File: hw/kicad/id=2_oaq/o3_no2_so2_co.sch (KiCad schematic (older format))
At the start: 54 parts, among them IC1 LPS22HB, IC2 SHTC1, IC3 TPS62740DSST, IC4 24AA02T-I_OT, IC5 nRF52840-QIAA-T, Q1 NMOS_DGS, Q2 NMOS_DGS, U1 SGPC3-2.5k, Y1 32MHZ, Y2 32.768K

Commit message: Update for OAQ
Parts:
- removed C1, C11, C15, C19, C20, C23, C24, C3, C5: 100nF, symbol C_Small
- removed C10, C6, C7, C9: 12pF, symbol C_Small
- removed C12, C14: 1uF, symbol C_Small
- removed C13, C17: 1pF, symbol C_Small
- removed C16, C25: 4.7uF, symbol C_Small
- removed C18: 47nF, symbol C_Small
- removed C2, C4: 10uF, Capacitors_SMD:C_0805, symbol C_Small
- removed C21: 100pF, symbol C_Small
- removed C22: 820pF, symbol C_Small
- removed C8: 1.2pF, symbol C_Small
- removed D1: red, symbol LED_Small
- removed D2: green, symbol LED_Small
- removed IC1: LPS22HB, LGA10R50P2X3_200X200X80, symbol LPS22HB
- removed IC2: SHTC1, SON100P200X200X7500-5N, symbol SHTC1
- removed IC3: TPS62740DSST, SON50P200X300X80-13N, symbol TPS62740DSST
- removed IC4: 24AA02T-I_OT, SOT95P270X145-5N, symbol 24AA02T-I_OT
- removed IC5: nRF52840-QIAA-T, AQFN73, symbol nRF52840-QIAA-T
- removed L1: 2.2uH, symbol L
- removed L2: 3.9nH, symbol L
- removed L3: 15nH, symbol L
- removed L4: 10uH, symbol L
- removed Q1, Q2: NMOS_DGS, symbol Q_NMOS_DGS
- removed R1: 10M, symbol R
- removed R10, R11, R12, R13, R5, R8, R9: 10k, symbol R_Small
- removed R2: 2M, symbol R
- removed R3, R4: 10k, symbol R
- removed R6, R7: 1k, symbol R_Small
- removed U1: SGPC3-2.5k, SON100P300X300X110-7N, symbol SGPC3-2.5k
- removed Y1: 32MHZ, FA128, symbol Q22FA12800025_FA-128_32_MHZ_8PF
- removed Y2: 32.768K, NX3215SA, symbol NX3215SA-32.768K-STD-MUA-9
- added C? (x8): 100nF, symbol C_Small
- added C? (x2): 1uF, symbol C_Small
- added IC? (x4): LMP91000SD_NOPB, SON50P400X400X80-15N, symbol LMP91000SD_NOPB
- added J? (x6): HDR_2x2mm, symbol Conn_01x02_Male
- added R? (x4): 100k, symbol R_Small
- added R? (x2): 500k, symbol R_Small
- added R? (x2): 1k, symbol R_Small
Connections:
- net labels added: 2V5, 2V7, CO, CO_EN, NO2, NO2_EN, O3, O3_EN, Reference_NO2, Reference_O3, SCL, SDA, SO2, SO2_EN, Working_NO2, Working_O3
- net labels removed: +1V8, ANT, Vbat
- wire segments 173 -> 102
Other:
- note added: "Ozone (NO2)\nSPEC Sensors"
- note added: "Ozone (O3)\nSPEC Sensors"
- note removed: "Battery power surveillance."
- note removed: "CO\n"
- note removed: "Configuration pin 0"
- note removed: "Configuration pin 1"
- note removed: "Configuration pin 2"
- note removed: "Configuration pin 3"
- note removed: "Configuration pin 4"
- note removed: "Configuration pin 5"
- note removed: "EEPROM"
- note removed: "H2S\n"
- note removed: "Module ID = 1 --> Indoor Air Quality Module (VOC)"
- note removed: "NO2\n"
- note removed: "O3"
- note removed: "Pressure Sensor"
- note removed: "SO2\n"
- note removed: "Temperature & Humidity Sensor"
- note removed: "UART RxD"
- note removed: "UART TxD"
- note removed: "VOC Sensor"
- note removed: "Vbat = 3 x AA Li-Fe 2.9Ah = 3 x 1.5V = 4.5V"

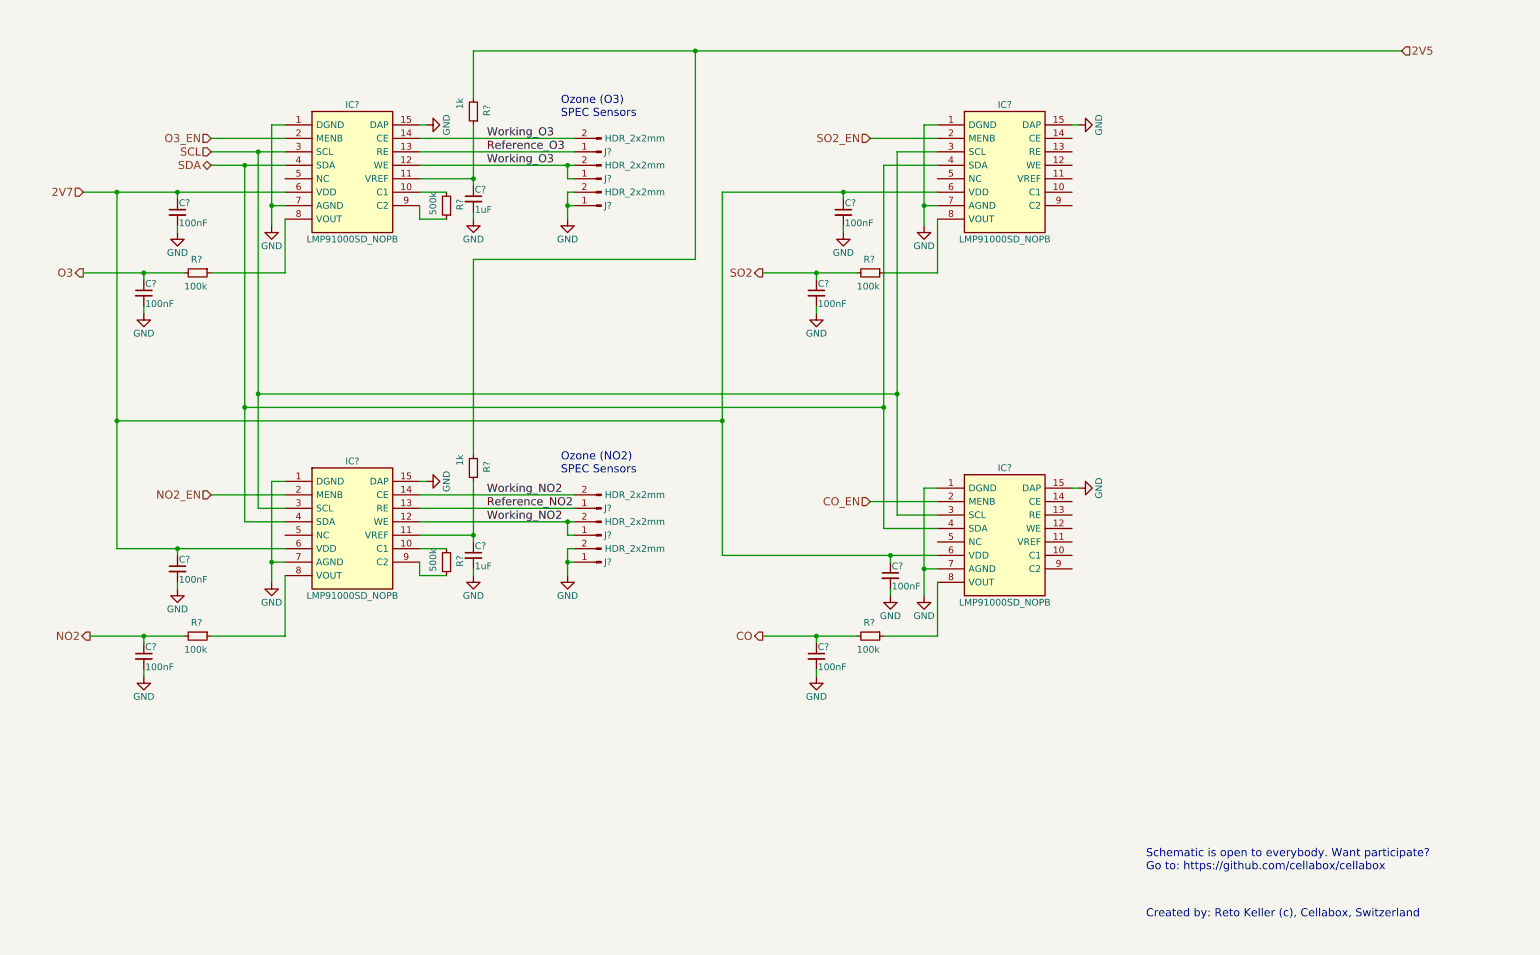
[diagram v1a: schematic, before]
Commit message: OAQ schematic updated: gains, ranges
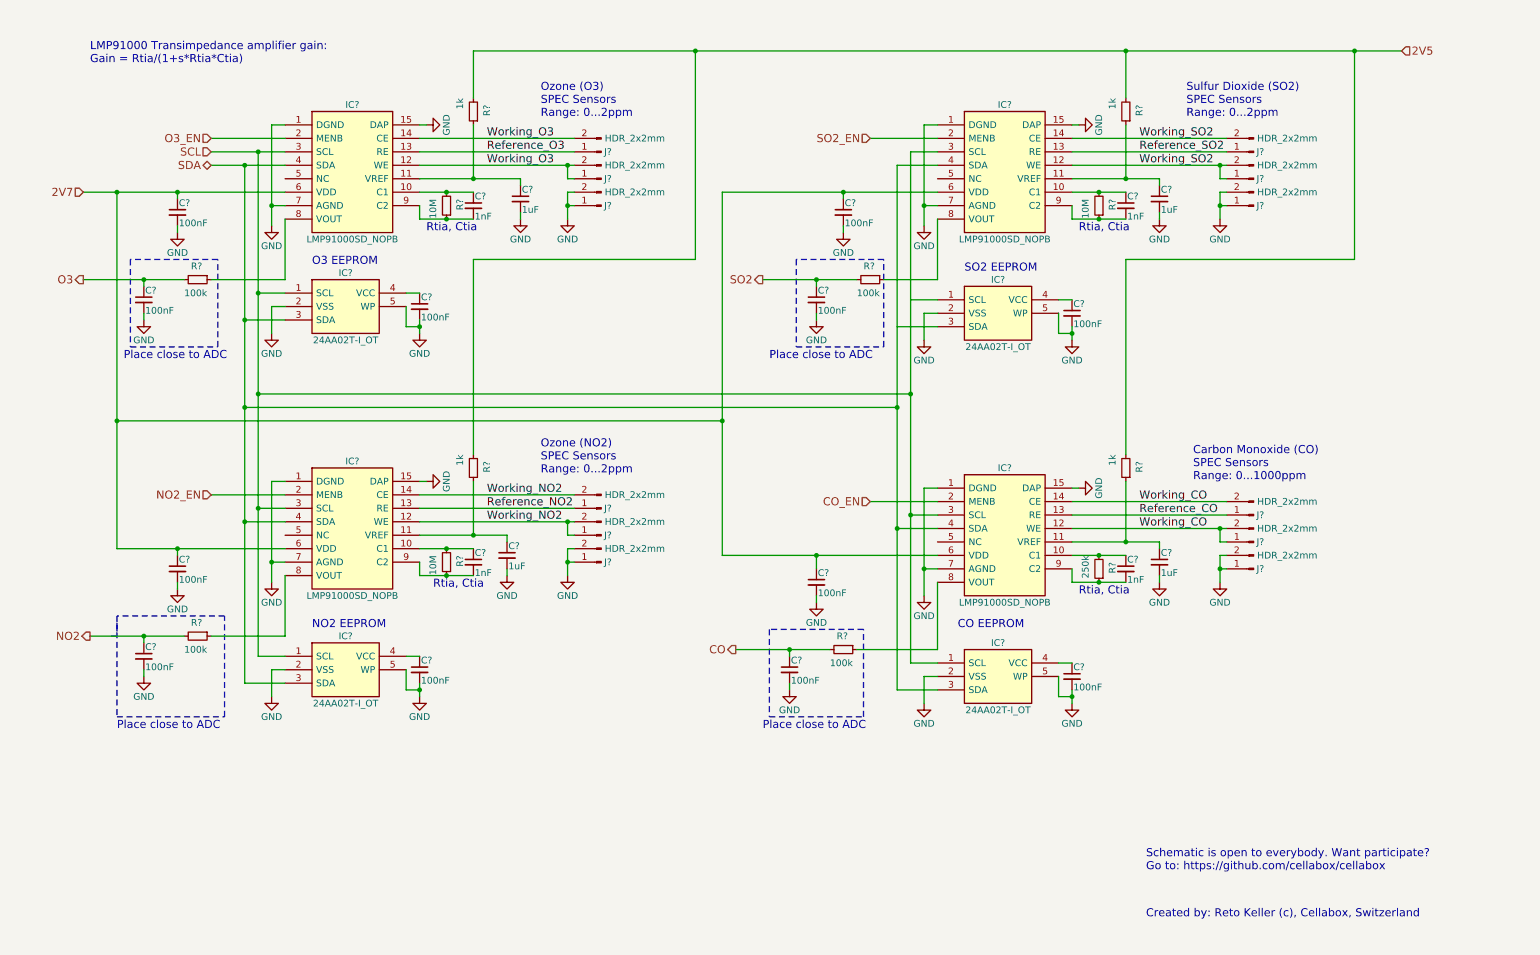
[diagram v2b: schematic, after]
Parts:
- added C? (x4): 100nF, symbol C_Small
- added C? (x4): 1nF, symbol C_Small
- added C? (x2): 1uF, symbol C_Small
- added IC? (x4): 24AA02T-I_OT, SOT95P270X145-5N, symbol 24AA02T-I_OT
- added J? (x6): HDR_2x2mm, symbol Conn_01x02_Male
- added R? (x2): 1k, symbol R_Small
- added R?: 250k, symbol R_Small
- added R?: 10M, symbol R_Small
- R? (x2): value 500k -> 10M
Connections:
- net 2V5: now also R?.2, R?.2
- net GND: now also C?.2, C?.2, C?.2, C?.2, C?.2, C?.2, IC?.2 (VSS), IC?.2 (VSS), IC?.2 (VSS), IC?.2 (VSS), IC?.5 (WP), IC?.5 (WP), IC?.5 (WP), IC?.5 (WP), J?.1 (Pin_1), J?.1 (Pin_1), J?.2 (Pin_2), J?.2 (Pin_2)
- net SCL: now also IC?.1 (SCL), IC?.1 (SCL), IC?.1 (SCL)
- net SDA: now also IC?.3 (SDA), IC?.3 (SDA), IC?.3 (SDA)
- net at IC?.10 (C1), R?.2: now also C?.1 (x2)
- net at IC?.9 (C2), R?.1: now also C?.2 (x2)
- net at IC?.10 (C1): now also C?.1, R?.2 (x2)
- net at IC?.11 (VREF): now also C?.1, R?.1 (x2)
- net Working_CO: now reaches IC?.12 (WE)
- net Working_CO: now also IC?.14 (CE), J?.1 (Pin_1), J?.2 (Pin_2), J?.2 (Pin_2)
- net Reference_CO: now reaches IC?.13 (RE)
- net Reference_CO: now also J?.1 (Pin_1)
- net at IC?.9 (C2): now also C?.2, R?.1 (x2)
- net Working_SO2: now reaches IC?.12 (WE)
- net Working_SO2: now also IC?.14 (CE), J?.1 (Pin_1), J?.2 (Pin_2), J?.2 (Pin_2)
- net Reference_SO2: now reaches IC?.13 (RE)
- net Reference_SO2: now also J?.1 (Pin_1)
- new net: C?.1, IC?.4 (VCC) (x4)
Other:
- note added: "CO EEPROM"
- note added: "Carbon Monoxide (CO)\nSPEC Sensors\nRange: 0...1000ppm"
- note added: "LMP91000 Transimpedance amplifier gain:\nGain = Rtia/(1+s*Rtia*Ctia)"
- note added: "NO2 EEPROM"
- note added: "O3 EEPROM"
- note added: "Ozone (NO2)\nSPEC Sensors\nRange: 0...2ppm"
- note added: "Ozone (O3)\nSPEC Sensors\nRange: 0...2ppm"
- note added: "Place close to ADC"
- note added: "Rtia, Ctia"
- note added: "SO2 EEPROM"
- note added: "Sulfur Dioxide (SO2)\nSPEC Sensors\nRange: 0...2ppm"
- note removed: "Ozone (NO2)\nSPEC Sensors"
- note removed: "Ozone (O3)\nSPEC Sensors"
- moved on the sheet: C?, R?

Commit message: Indoor PM2.5 module. Schematic added.
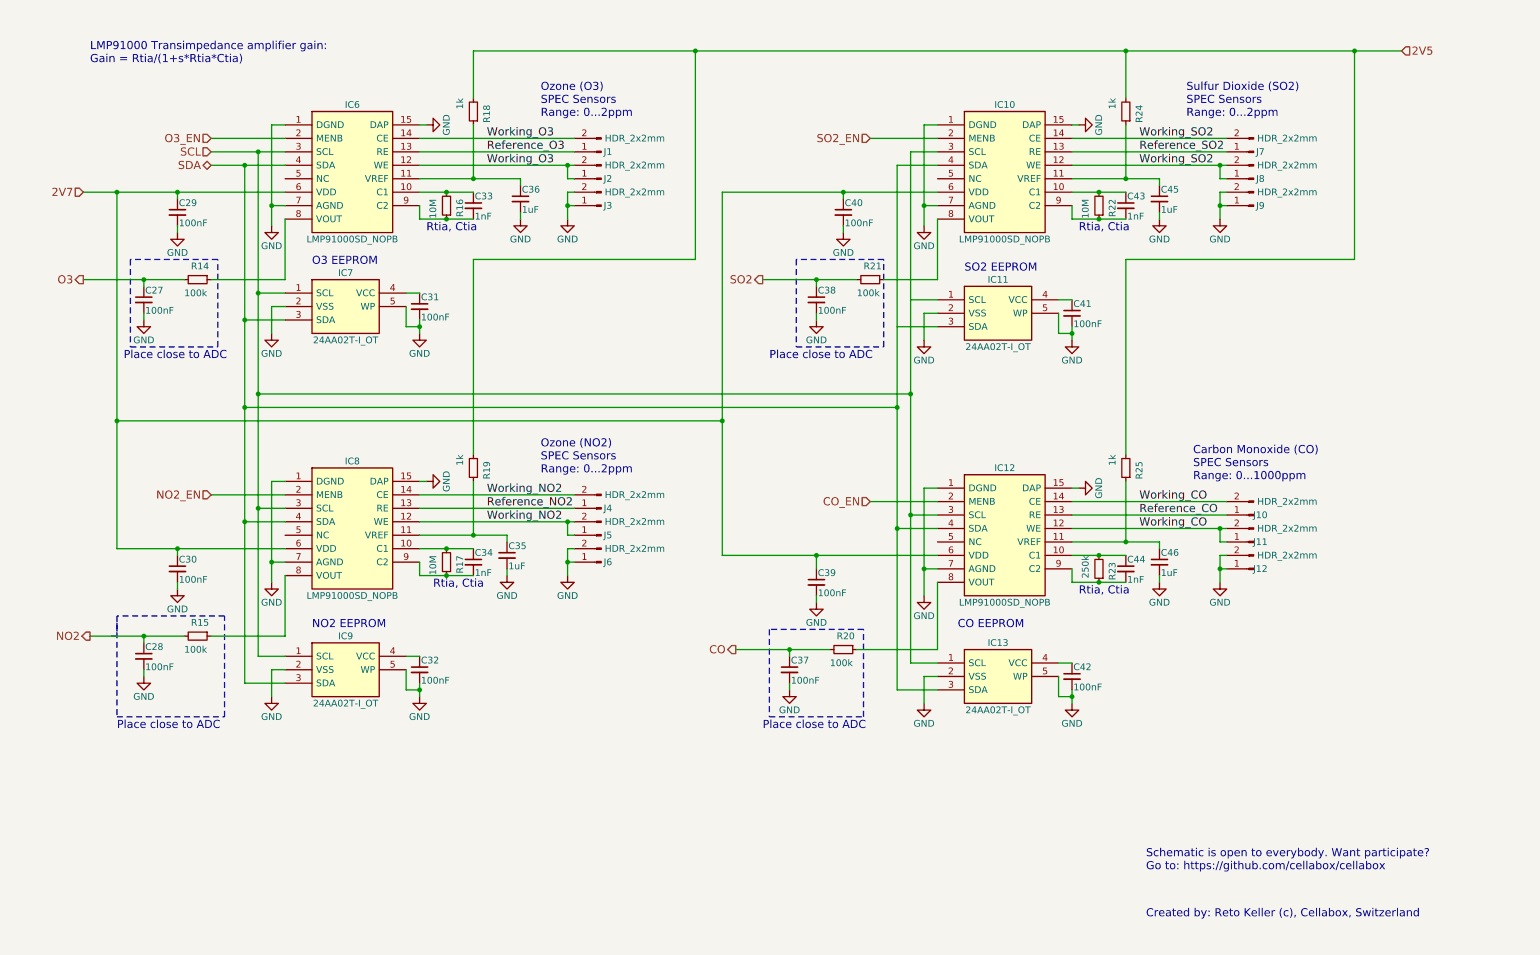
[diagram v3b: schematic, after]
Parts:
- gave numbers to parts that had none: 52
